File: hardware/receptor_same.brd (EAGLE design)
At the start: 100 x 80 mm, 66 parts, among them J1 ICSP, J2 SERIAL, J3 GPIO, J4 AUX-POWER, K1 HLS8L-DC5V, Q1 MMBT3904LT1G, U1 ATMEGA328P_TQFP, U2 SI4707, U3 TPA6111A2DR, U4 MCP16301/H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

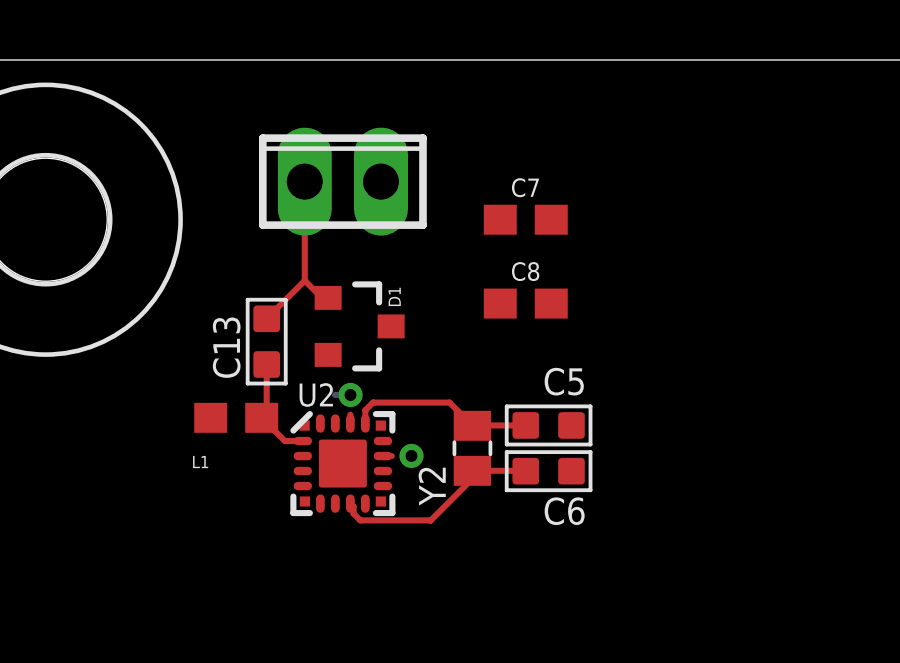
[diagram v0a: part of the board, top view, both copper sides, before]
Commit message: avances si4707 y audio
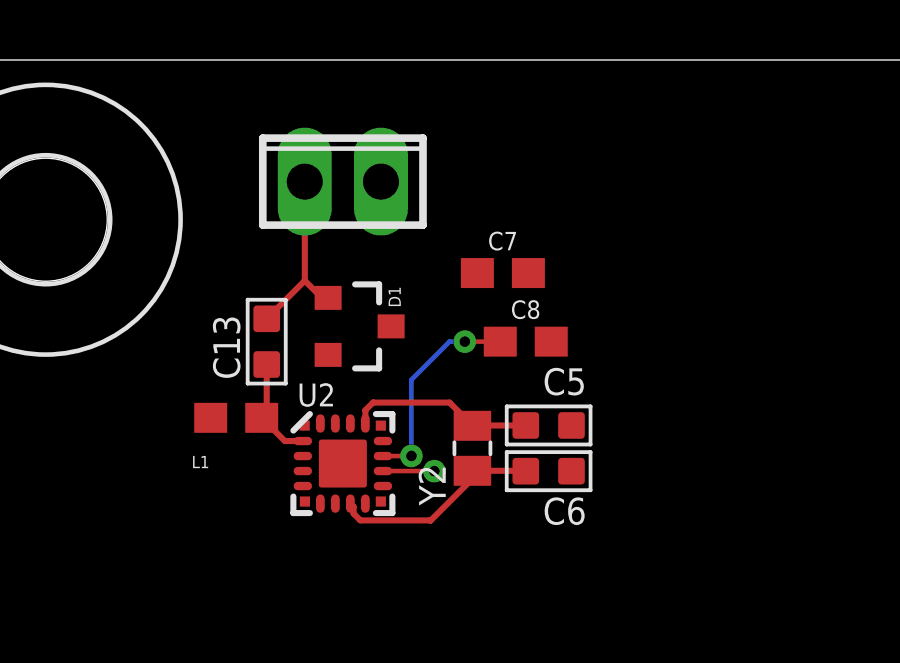
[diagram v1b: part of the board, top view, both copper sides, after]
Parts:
- moved C7 1.93 mm to (20.6, 72.9)
- moved C8 1.27 mm to (21.3, 70.6)
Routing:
- net N$23: track 0.00 -> 4.84 mm
- net AUDIO-L: track 0.29 -> 2.13 mm
- net AUDIO-R: track 0.00 -> 1.71 mm
- net N$32: track 0.81 -> 0.00 mm

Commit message: avances ruteo si + amp
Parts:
- moved R8 96.3 mm to (31.5, 71.9), turned to 270 degrees
- moved L2 93.6 mm to (26.2, 76.5), turned to 90 degrees
- moved R7 88.9 mm to (30.2, 62.7), turned to 270 degrees
- moved U3 81.8 mm to (31.5, 67.3)
- moved C10 81.5 mm to (37.5, 70.5), turned to 270 degrees
- moved R6 79.0 mm to (23.7, 73.0), turned to 90 degrees
- moved C4 77.4 mm to (18.9, 62.9)
- moved R5 74.2 mm to (24.5, 70.4), turned to 90 degrees
- moved C3 69.7 mm to (16.4, 62.9)
- moved C9 61.2 mm to (25.3, 62.0)
- moved L3 60.8 mm to (36.8, 76.6), turned to 90 degrees
- moved C12 53.7 mm to (27.9, 70.9), turned to 180 degrees
- moved C11 53.1 mm to (32.6, 61.5)
- moved J1 50.5 mm to (37.8, 51.9)
- moved Y1 42.6 mm to (9.53, 49.7)
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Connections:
- net N$11: now also C10.A; no longer C9.A
- net N$13: now also C9.A; no longer C10.A
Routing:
- net N$11: track 0.00 -> 20.1 mm
- net N$14: track 0.00 -> 15.5 mm, vias 0 -> 2
- net N$13: track 0.00 -> 14.1 mm, vias 0 -> 2
- net N$10: track 0.00 -> 12.2 mm
- net N$12: track 0.00 -> 10.3 mm
- net +3V3: track 0.00 -> 7.13 mm, vias 0 -> 2
- net AUDIO-L: track 2.13 -> 7.41 mm, vias 0 -> 2
- net N$23: track 4.84 -> 0.00 mm, vias 1 -> 0
- net AUDIO-R: track 1.71 -> 6.45 mm, vias 0 -> 2
- net N$17: track 0.00 -> 4.62 mm
- net N$16: track 0.00 -> 2.83 mm
- net N$15: track 0.00 -> 2.81 mm
- net N$9: track 0.00 -> 2.49 mm
- net N$8: track 0.00 -> 2.36 mm
- net N$7: track 0.00 -> 2.12 mm
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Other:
- board text added: "GND"
- board text added: "L G R"

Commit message: avances pcba
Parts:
- X1: value ANT -> ANTENNA
- moved H4 183.1 mm to (96.5, 55.9)
- moved H3 161.1 mm to (96.5, 5.08)
- moved L4 160.4 mm to (87.4, 64.1)
- moved U4 147.1 mm to (79.0, 68.1)
- moved R13 141.8 mm to (88.0, 38.0)
- moved R12 139.0 mm to (89.7, 31.9)
- moved D4 139.0 mm to (85.3, 52.6)
- moved D6 134.8 mm to (70.1, 11.6), turned to 270 degrees
- moved U5 122.2 mm to (77.2, 54.2)
- moved C15 120.1 mm to (84.3, 72.3)
- moved C16 120.1 mm to (79.2, 72.3)
- moved C17 120.1 mm to (74.2, 72.3)
- moved R14 120.1 mm to (99.6, 68.5)
- moved R15 120.1 mm to (94.5, 68.5)
- moved R4 120.1 mm to (76.7, 63.4)
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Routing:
- net N$26: track 0.00 -> 29.0 mm
- net RTS: track 0.00 -> 25.4 mm, vias 0 -> 1
- net N$29: track 0.00 -> 22.5 mm
- net RXD: track 0.00 -> 22.2 mm, vias 0 -> 2
- net TXD: track 0.00 -> 20.5 mm, vias 0 -> 1
- net CTS: track 0.00 -> 19.2 mm, vias 0 -> 1
- net N$14: track 15.5 -> 2.88 mm, vias 2 -> 0
- net N$15: track 2.81 -> 13.7 mm, vias 0 -> 1
- net N$28: track 0.00 -> 8.27 mm
- net +3V3: track 7.13 -> 13.2 mm
- net SCL: track 0.00 -> 6.02 mm
- net N$2: track 0.00 -> 4.38 mm
- net SDA: track 0.00 -> 3.21 mm
- net RST-AVR: track 0.00 -> 3.19 mm
- net N$1: track 0.00 -> 2.95 mm
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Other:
- board size 100 x 80 mm -> 101.6 x 61 mm
- board text removed: "GND"
- board text removed: "L G R"

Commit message: pcb terminado
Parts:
- moved R4 64.8 mm to (13.8, 47.6), turned to 90 degrees
- moved J4 55.1 mm to (3.05, 38.1), turned to 180 degrees
- moved R11 43.9 mm to (71.1, 33.8)
- moved C15 42.0 mm to (50.0, 48.1), turned to 180 degrees
- moved R14 39.1 mm to (64.8, 50.7)
- moved X5 37.2 mm to (59.8, 57.1)
- moved R15 37.2 mm to (61.8, 50.7)
- moved D4 37.0 mm to (48.3, 51.1)
- moved L4 36.8 mm to (55.6, 45.5)
- moved C18 34.2 mm to (45.0, 48.0), turned to 180 degrees
- moved U5 31.8 mm to (47.2, 43.7), turned to 180 degrees
- moved C16 29.9 mm to (64.8, 46.1), turned to 180 degrees
- moved C17 28.9 mm to (61.8, 46.1), turned to 180 degrees
- moved U4 27.8 mm to (55.9, 52.6)
- moved K1 24.1 mm to (58.4, 11.4)
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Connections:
- net N$15 renamed L
- net N$16 renamed R
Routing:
- net +3V3: track 13.2 -> 233.9 mm, vias 2 -> 10
- net +5V: track 0.00 -> 165.6 mm, vias 0 -> 6
- net BTN: track 0.00 -> 66.5 mm, vias 0 -> 2
- net LED-4: track 0.00 -> 66.2 mm
- net LED-3: track 0.00 -> 65.1 mm
- net RST-SI: track 0.00 -> 46.0 mm
- net MISO: track 0.00 -> 34.6 mm
- net A6: track 1.50 -> 35.3 mm, vias 1 -> 2
- net MOSI: track 0.00 -> 31.5 mm
- net INT-SI: track 1.54 -> 32.3 mm, vias 1 -> 2
- net A0: track 0.00 -> 29.0 mm, vias 0 -> 1
- net RELAY: track 0.00 -> 28.4 mm, vias 0 -> 2
- net A1: track 0.00 -> 26.7 mm, vias 0 -> 1
- net A3: track 0.00 -> 26.5 mm, vias 0 -> 1
- net A2: track 0.00 -> 24.7 mm, vias 0 -> 1
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- added copper zone on layer 1, net GND
- added copper zone on layer 16, net GND
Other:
- board size 101.6 x 61 mm -> 78.7 x 61 mm
- board text added: "Manuel Rabade (2019)"
